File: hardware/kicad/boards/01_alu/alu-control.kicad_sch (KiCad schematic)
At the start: 8 parts, among them U153 KM28C64A, U154 KM28C64A, U155 74AHC541, U156 74AHC541

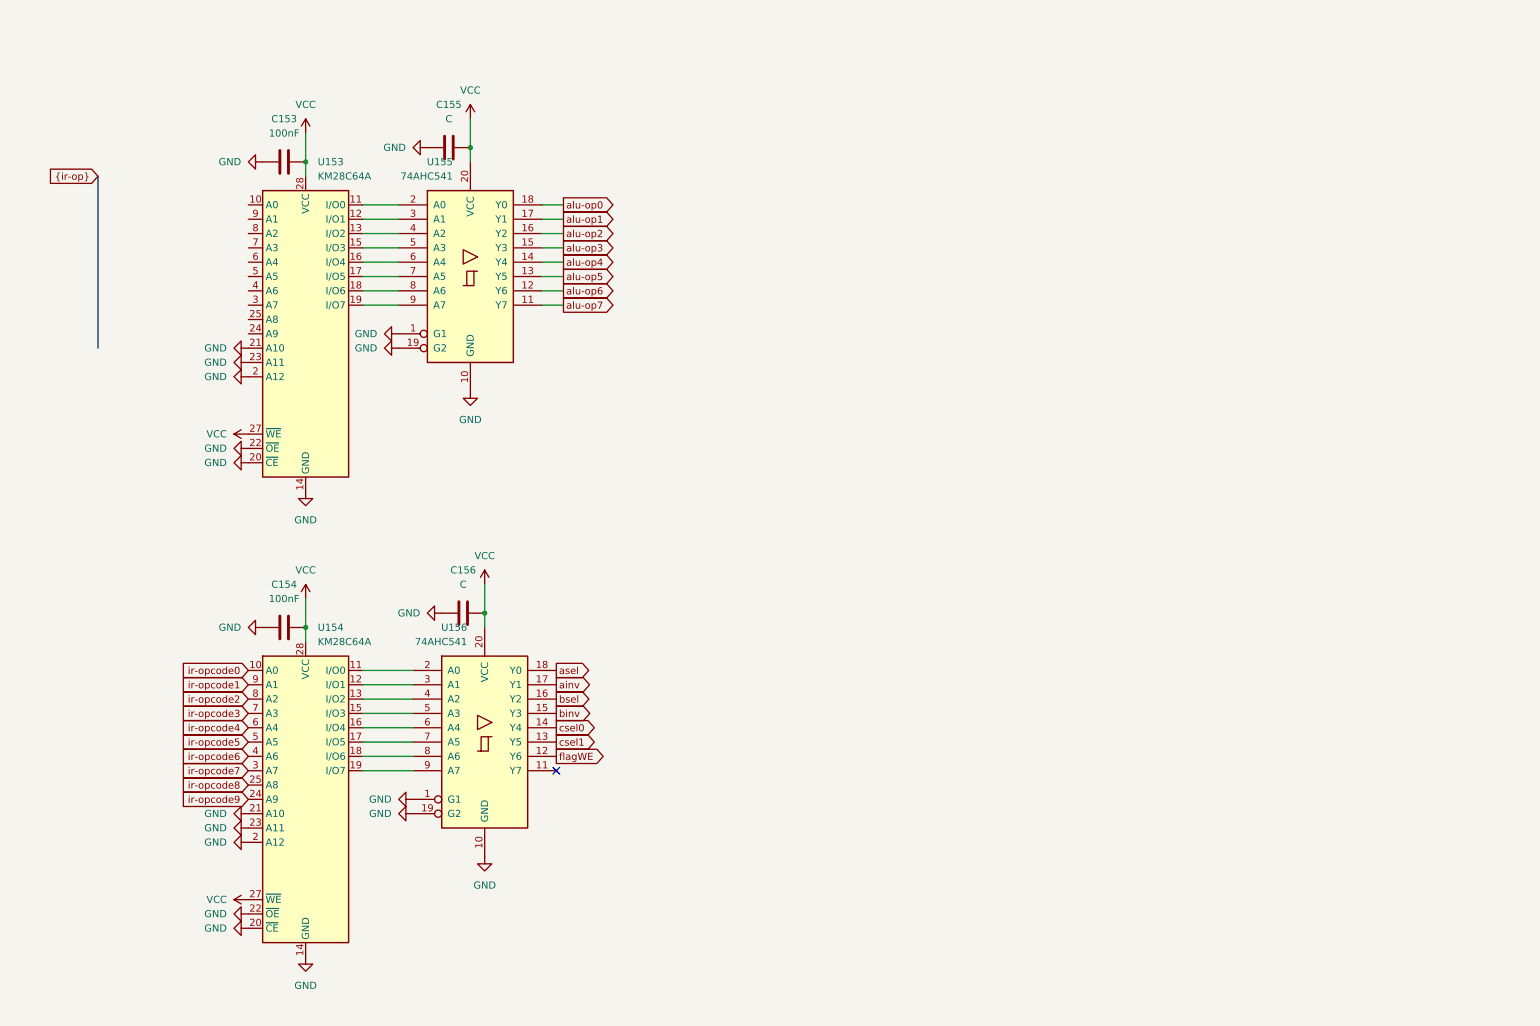
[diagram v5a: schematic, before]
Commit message: feat: designed ALU board with 0 ERC errors or warnings 🎉
Final review of logical correctness and footprints and then routing begins
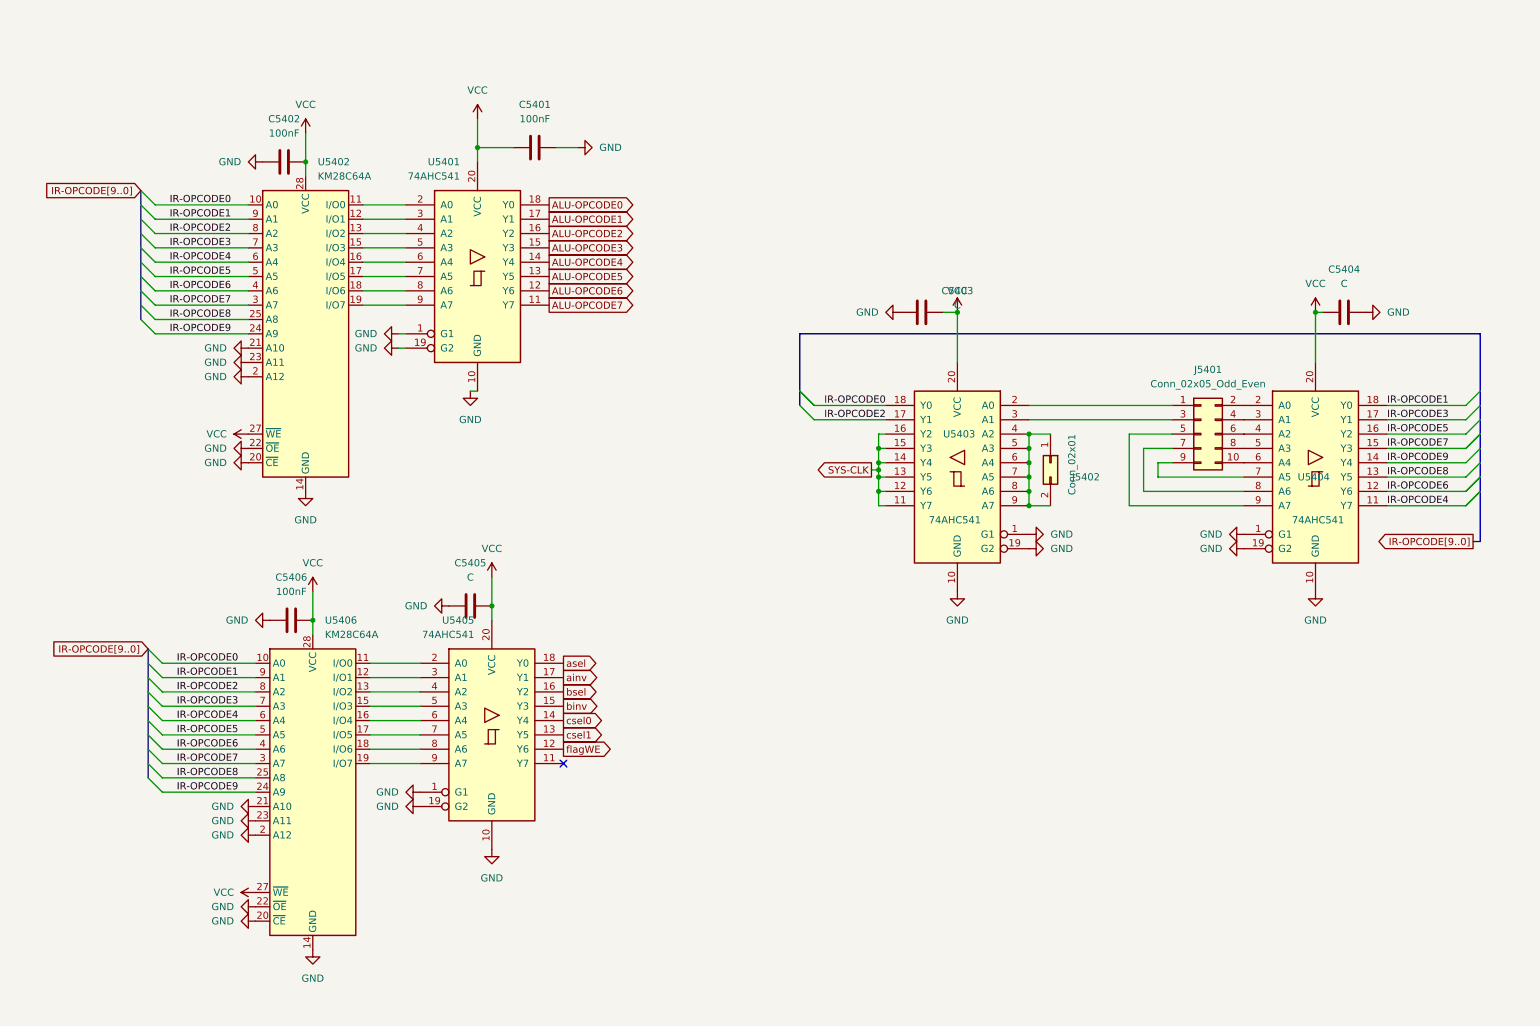
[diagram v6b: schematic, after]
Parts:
- removed C154: 100nF, Capacitor_SMD:C_0805_2012Metric, symbol Device:C
- removed C155: C, Capacitor_SMD:C_0805_2012Metric, symbol Device:C
- removed U154: KM28C64A, Package_DIP:DIP-28_W15.24mm, symbol Memory_EEPROM:KM28C64A
- added C5401, C5406: 100nF, Capacitor_SMD:C_0805_2012Metric, symbol Device:C
- added C5403, C5404: C, Capacitor_SMD:C_0805_2012Metric, symbol Device:C
- added J5401: Conn_02x05_Odd_Even, Connector_PinHeader_2.54mm:PinHeader_2x05_P2.54mm_Vertical, symbol Connector_Generic:Conn_02x05_Odd_Even
- added J5402: Conn_02x01, Connector_PinHeader_2.54mm:PinHeader_2x01_P2.54mm_Horizontal, symbol Connector_Generic:Conn_02x01
- added U5403, U5404: 74AHC541, Package_SO:SOIC-20W_7.5x12.8mm_P1.27mm, symbol 74xx:74AHC541
- added U5406: KM28C64A, Package_DIP:DIP-28_W15.24mm, symbol Memory_EEPROM:KM28C64A
- renumbered C153 to C5402, C156 to C5405, U155 to U5401, U153 to U5402, U156 to U5405
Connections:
- net GND: now also C5401.2, C5403.2, C5404.1, C5406.1, U5403.1 (G1), U5403.10 (GND), U5403.19 (G2), U5404.1 (G1), U5404.10 (GND), U5404.19 (G2), U5406.14 (GND), U5406.2 (A12), U5406.20 (~{CE}), U5406.21 (A10), U5406.22 (~{OE}), U5406.23 (A11)
- net VCC: now also C5401.1, C5403.1, C5404.2, C5406.2, U5403.20 (VCC), U5404.20 (VCC), U5406.27 (~{WE}), U5406.28 (VCC)
- net IR-OPCODE0: now reaches U5402.10 (A0)
- net IR-OPCODE0: now also U5403.18 (Y0), U5406.10 (A0)
- net IR-OPCODE9: now reaches U5402.24 (A9)
- net IR-OPCODE9: now also U5404.14 (Y4), U5406.24 (A9)
- net IR-OPCODE8: now reaches U5402.25 (A8)
- net IR-OPCODE8: now also U5404.13 (Y5), U5406.25 (A8)
- net IR-OPCODE7: now reaches U5402.3 (A7)
- net IR-OPCODE7: now also U5404.15 (Y3), U5406.3 (A7)
- net IR-OPCODE6: now reaches U5402.4 (A6)
- net IR-OPCODE6: now also U5404.12 (Y6), U5406.4 (A6)
- net IR-OPCODE5: now reaches U5402.5 (A5)
- net IR-OPCODE5: now also U5404.16 (Y2), U5406.5 (A5)
- net IR-OPCODE4: now reaches U5402.6 (A4)
- net IR-OPCODE4: now also U5404.11 (Y7), U5406.6 (A4)
- net IR-OPCODE3: now reaches U5402.7 (A3)
- net IR-OPCODE3: now also U5404.17 (Y1), U5406.7 (A3)
- net IR-OPCODE2: now reaches U5402.8 (A2)
- net IR-OPCODE2: now also U5403.17 (Y1), U5406.8 (A2)
- net IR-OPCODE1: now reaches U5402.9 (A1)
- net IR-OPCODE1: now also U5404.18 (Y0), U5406.9 (A1)
- net at U5405.2 (A0): now also U5406.11 (I/O0)
- net at U5405.3 (A1): now also U5406.12 (I/O1)
- net at U5405.4 (A2): now also U5406.13 (I/O2)
- net at U5405.5 (A3): now also U5406.15 (I/O3)
- net at U5405.6 (A4): now also U5406.16 (I/O4)
- net at U5405.7 (A5): now also U5406.17 (I/O5)
- net at U5405.8 (A6): now also U5406.18 (I/O6)
- net at U5405.9 (A7): now also U5406.19 (I/O7)
- net alu-op0 renamed ALU-OPCODE0
- net alu-op1 renamed ALU-OPCODE1
- net alu-op2 renamed ALU-OPCODE2
- net alu-op3 renamed ALU-OPCODE3
- net alu-op4 renamed ALU-OPCODE4
- net alu-op5 renamed ALU-OPCODE5
- net alu-op6 renamed ALU-OPCODE6
- net alu-op7 renamed ALU-OPCODE7
- new net: J5401.1 (Pin_1), U5403.2 (A0)
- new net: J5401.10 (Pin_10), U5404.6 (A4)
- new net: J5401.2 (Pin_2), U5404.2 (A0)
- new net: J5401.3 (Pin_3), U5403.3 (A1)
- new net: J5401.4 (Pin_4), U5404.3 (A1)
- new net: J5401.5 (Pin_5), U5404.9 (A7)
- new net: J5401.6 (Pin_6), U5404.4 (A2)
- new net: J5401.7 (Pin_7), U5404.8 (A6)
- new net: J5401.8 (Pin_8), U5404.5 (A3)
- new net: J5401.9 (Pin_9), U5404.7 (A5)
- new net: J5402.1 (Pin_1), J5402.2 (Pin_2), U5403.4 (A2), U5403.5 (A3), U5403.6 (A4), U5403.7 (A5), U5403.8 (A6), U5403.9 (A7)
- new net SYS-CLK: U5403.11 (Y7), U5403.12 (Y6), U5403.13 (Y5), U5403.14 (Y4), U5403.15 (Y3), U5403.16 (Y2)
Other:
- moved on the sheet: C5405, U5401, U5405

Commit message: arch: added LEDs, override switches; fixed errors and warnings to 0
ready for routing after logical coherence check
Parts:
- added SW14, SW15: SW_DIP_x08, Button_Switch_THT:SW_DIP_SPSTx08_Slide_9.78x22.5mm_W7.62mm_P2.54mm, symbol Switch:SW_DIP_x08
- added SW16: SW_Slide_DPDT, Button_Switch_SMD:SW_DPDT_CK_JS202011JCQN, symbol Switch:SW_Slide_DPDT
- renumbered C5402 to C150, C5406 to C151, C5405 to C152, C5401 to C153, C5403 to C154, C5404 to C155, J5402 to J7, J5401 to J8, U5402 to U150, U5406 to U151, U5401 to U152, U5405 to U153, U5403 to U154, U5404 to U155
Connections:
- net ALU-OPCODE0: now also SW14.16
- net ALU-OPCODE1: now also SW14.15
- net ALU-OPCODE2: now also SW14.14
- net ALU-OPCODE3: now also SW14.13
- net ALU-OPCODE4: now also SW14.12
- net ALU-OPCODE5: now also SW14.11
- net ALU-OPCODE6: now also SW14.10
- net ALU-OPCODE7: now also SW14.9
- net GND: now also SW16.3 (C); no longer U152.1 (G1), U152.19 (G2), U153.1 (G1), U153.19 (G2)
- net VCC: now also SW16.1 (A), SW16.6 (C)
- net ainv: now also SW15.15
- net asel: now also SW15.16
- net binv: now also SW15.13
- net bsel: now also SW15.14
- net csel0: now also SW15.12
- net csel1: now also SW15.11
- net flagWE: now also SW15.10
- new net Ctrl_EN: SW16.2 (B), U153.1 (G1), U153.19 (G2)
- new net Override: SW15.1, SW15.2, SW15.3, SW15.4, SW15.5, SW15.6, SW15.7, SW15.8, U152.1 (G1), U152.19 (G2)
- new net SW_EN: SW14.1, SW14.2, SW14.3, SW14.4, SW14.5, SW14.6, SW14.7, SW14.8, SW16.5 (B)
- no-connect marks 1 -> 3

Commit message: chore: cleanup and annotation  of alu subboards; hygiene before routing
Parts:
- renumbered C150 to C155, C151 to C156, C152 to C157, C153 to C158, C154 to C159, C155 to C160, U150 to U155, U151 to U156, U152 to U157, U153 to U158, U154 to U159, U155 to U160
